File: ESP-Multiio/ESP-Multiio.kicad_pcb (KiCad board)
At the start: 2 copper layers, 75 x 68 mm, 50 parts, among them J1 Conn_01x10, Q1 BC337, SW1 SW_SPDT_MSM, SW2 SW_SPDT_MSM, SW3 SW_SPDT_MSM, SW4 SW_SPDT_MSM, U1 WeMos_D1_mini, U2 MCP23017_SP, U4 TSOP1838

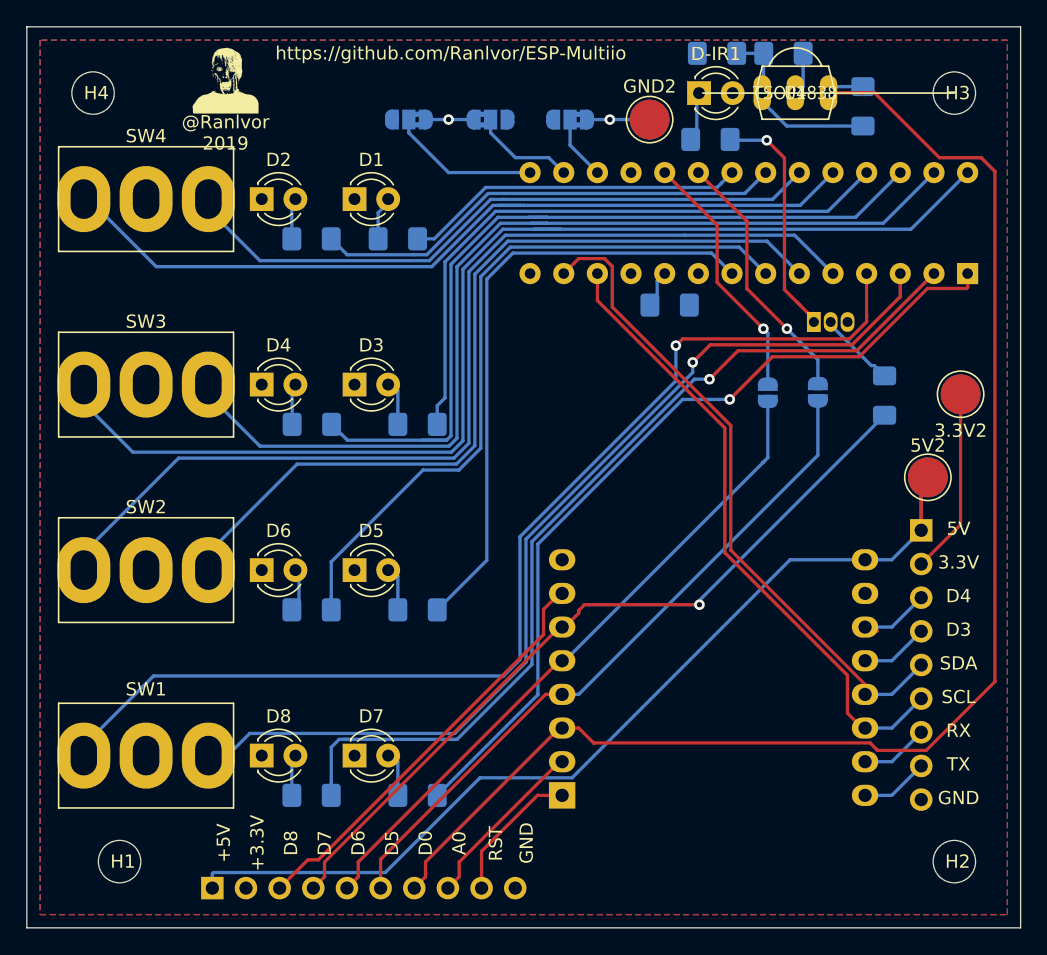
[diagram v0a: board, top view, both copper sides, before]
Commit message: Flip two parts on board to lower casing hight
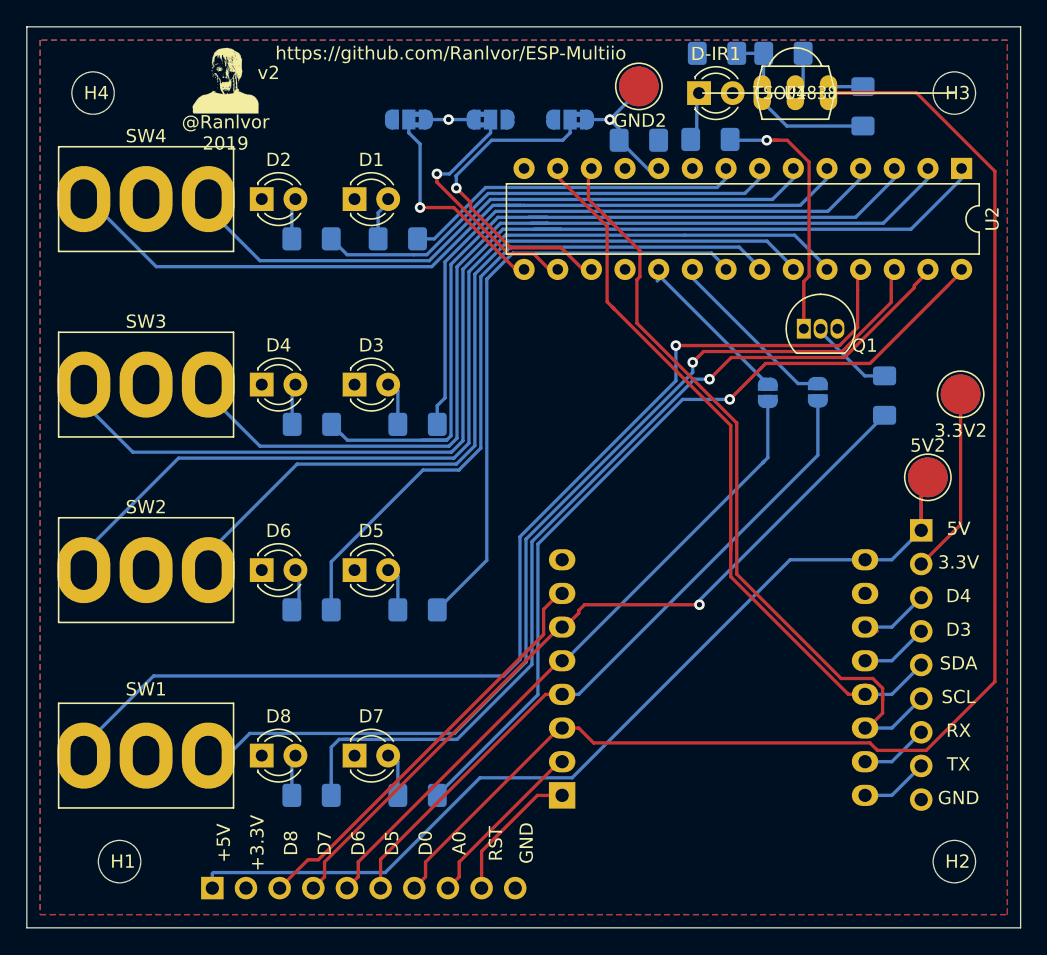
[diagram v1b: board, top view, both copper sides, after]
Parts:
- Q1, U2: moved to F.Cu
- moved C1 12.7 mm to (123.2, 35.6)
- moved U2 7.94 mm to (147.5, 37.7), turned to 270 degrees
- moved GND1 2.63 mm to (123.2, 31.5)
- moved GND2 2.63 mm to (123.2, 31.5)
- moved Q1 0.92 mm to (135.6, 49.8)
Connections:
- U2 pad 1: /GPB0 -> /GPA7
- U2 pad 11: Net-(U2-Pad11) -> (no net)
- U2 pad 14: Net-(U2-Pad14) -> (no net)
- U2 pad 2: /GPB1 -> /GPA6
- U2 pad 21: /GPA0 -> /GPB7
- U2 pad 22: /GPA1 -> /GPB6
- U2 pad 23: /GPA2 -> /GPB5
- U2 pad 24: /GPA3 -> /GPB4
- U2 pad 25: /GPA4 -> /GPB3
- U2 pad 26: /GPA5 -> /GPB2
- U2 pad 27: /GPA6 -> /GPB1
- U2 pad 28: /GPA7 -> /GPB0
- U2 pad 3: /GPB2 -> /GPA5
- U2 pad 4: /GPB3 -> /GPA4
- U2 pad 5: /GPB4 -> /GPA3
- U2 pad 6: /GPB5 -> /GPA2
- U2 pad 7: /GPB6 -> /GPA1
- U2 pad 8: /GPB7 -> /GPA0
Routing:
- net Net-(A2-Pad2): track 4.85 -> 24.8 mm, vias 0 -> 1
- net SCL: track 49.0 -> 60.4 mm
- net Net-(A1-Pad2): track 8.33 -> 19.2 mm, vias 0 -> 1
- net Net-(JP-INTA1-Pad2): track 21.3 -> 13.1 mm, vias 1 -> 0
- net SDA: track 50.0 -> 56.7 mm
- net Net-(JP-INTB1-Pad2): track 19.3 -> 12.8 mm, vias 1 -> 0
- net Net-(A0-Pad2): track 11.4 -> 16.7 mm, vias 0 -> 1
- net GND: track 15.7 -> 19.5 mm
- net /D0: track 109.6 -> 113.0 mm
- net Net-(Q1-Pad1): track 18.4 -> 19.7 mm
- net /GPB0: track 63.6 -> 62.3 mm
- net /GPB1: track 69.7 -> 69.1 mm
- net Net-(Q1-Pad2): track 5.88 -> 6.43 mm
- net /GPB3: track 83.7 -> 83.2 mm
- net /GPB2: track 77.6 -> 77.0 mm
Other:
- board text added: "v2"
